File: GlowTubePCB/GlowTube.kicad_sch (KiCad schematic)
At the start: 41 parts, among them J1 Conn_01x07, P1 Solder_Pad, P2 Solder_Pad, P3 Solder_Pad, P4 Solder_Pad, P5 Solder_Pad, P6 Solder_Pad, SW1 TS-1185EC-C-D-B, SW2 TS-1185EC-C-D-B, U1 SN74LVC2T45DCUR, U2 ESP32-WROOM-32E, U3 CP2102-GMR, U4 BL1117-33CX, U5 UMH3N, U6 MSM261D4030H1CPM, U7 SS54, U8 SS54

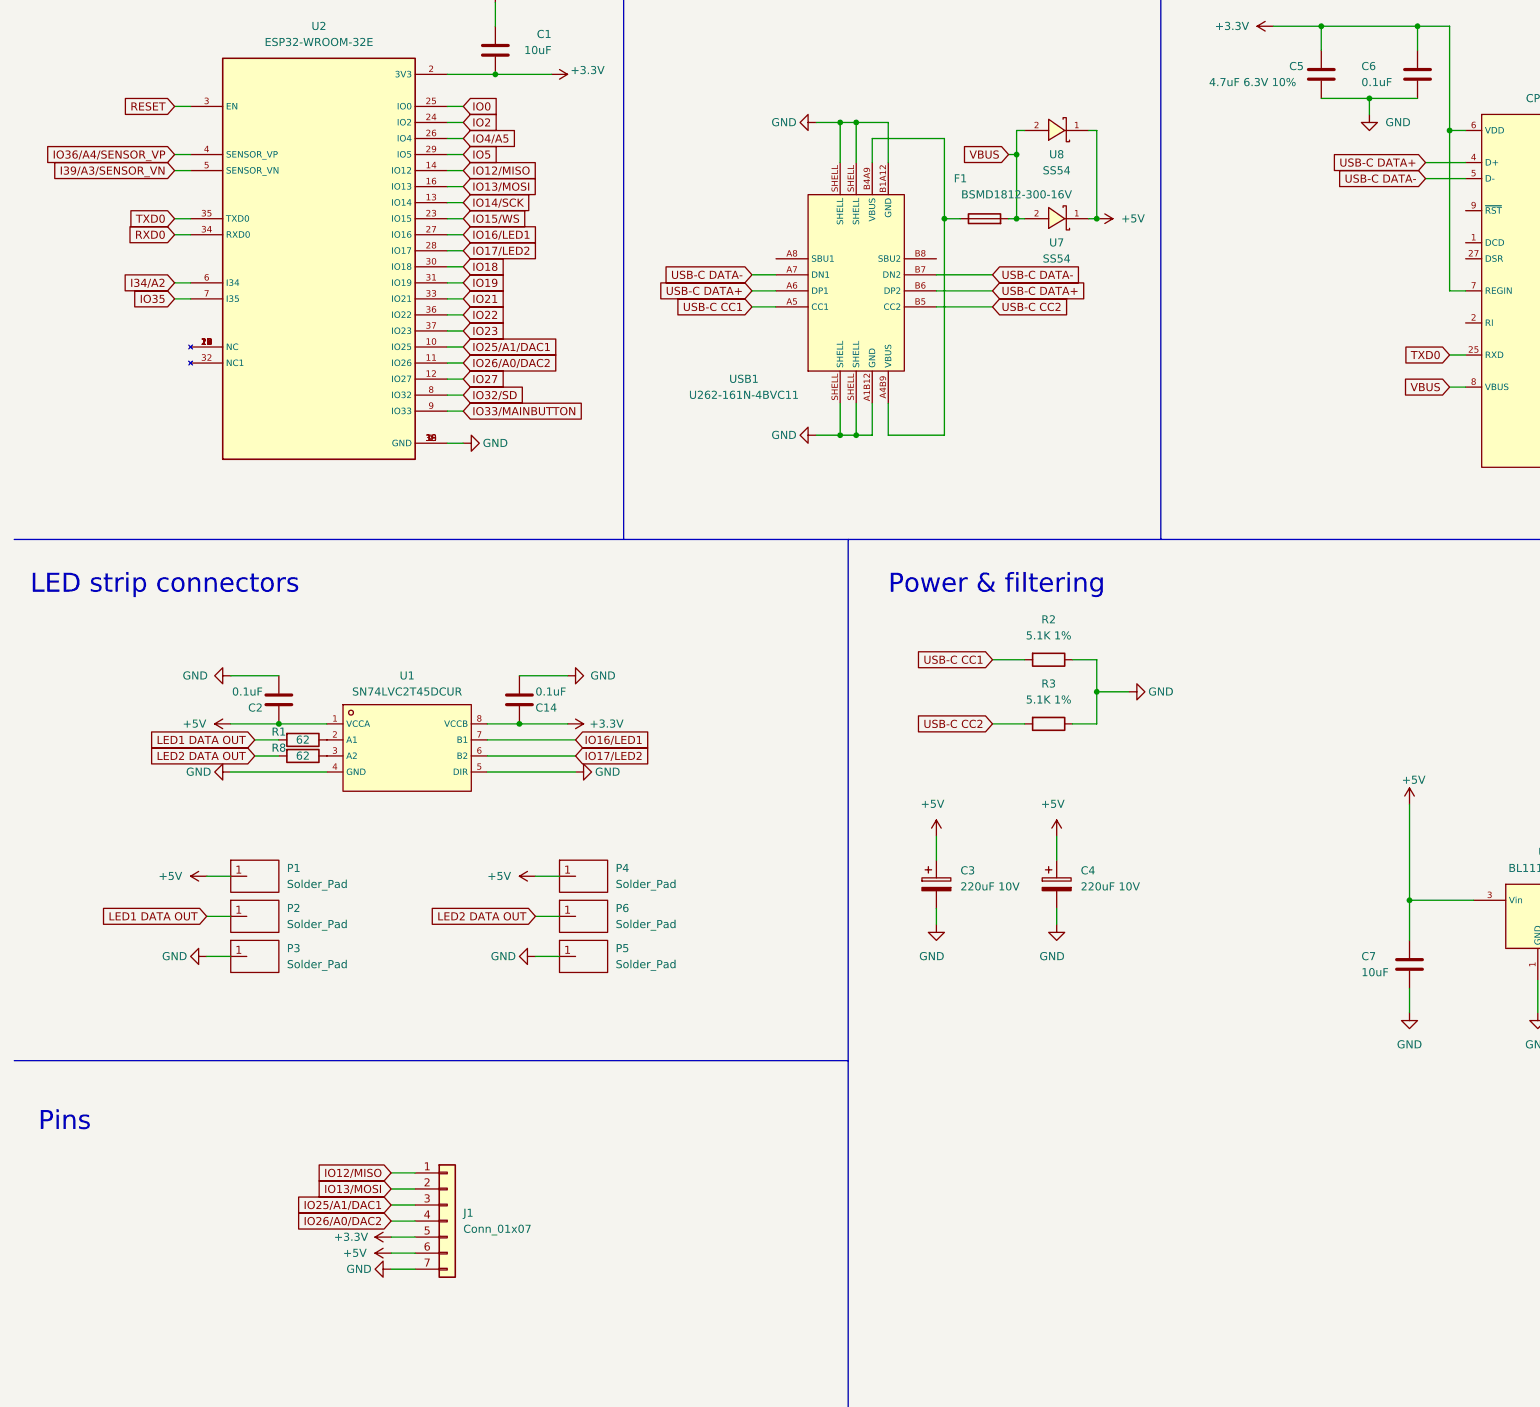
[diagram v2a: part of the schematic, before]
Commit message: added option to disconnect leds from power
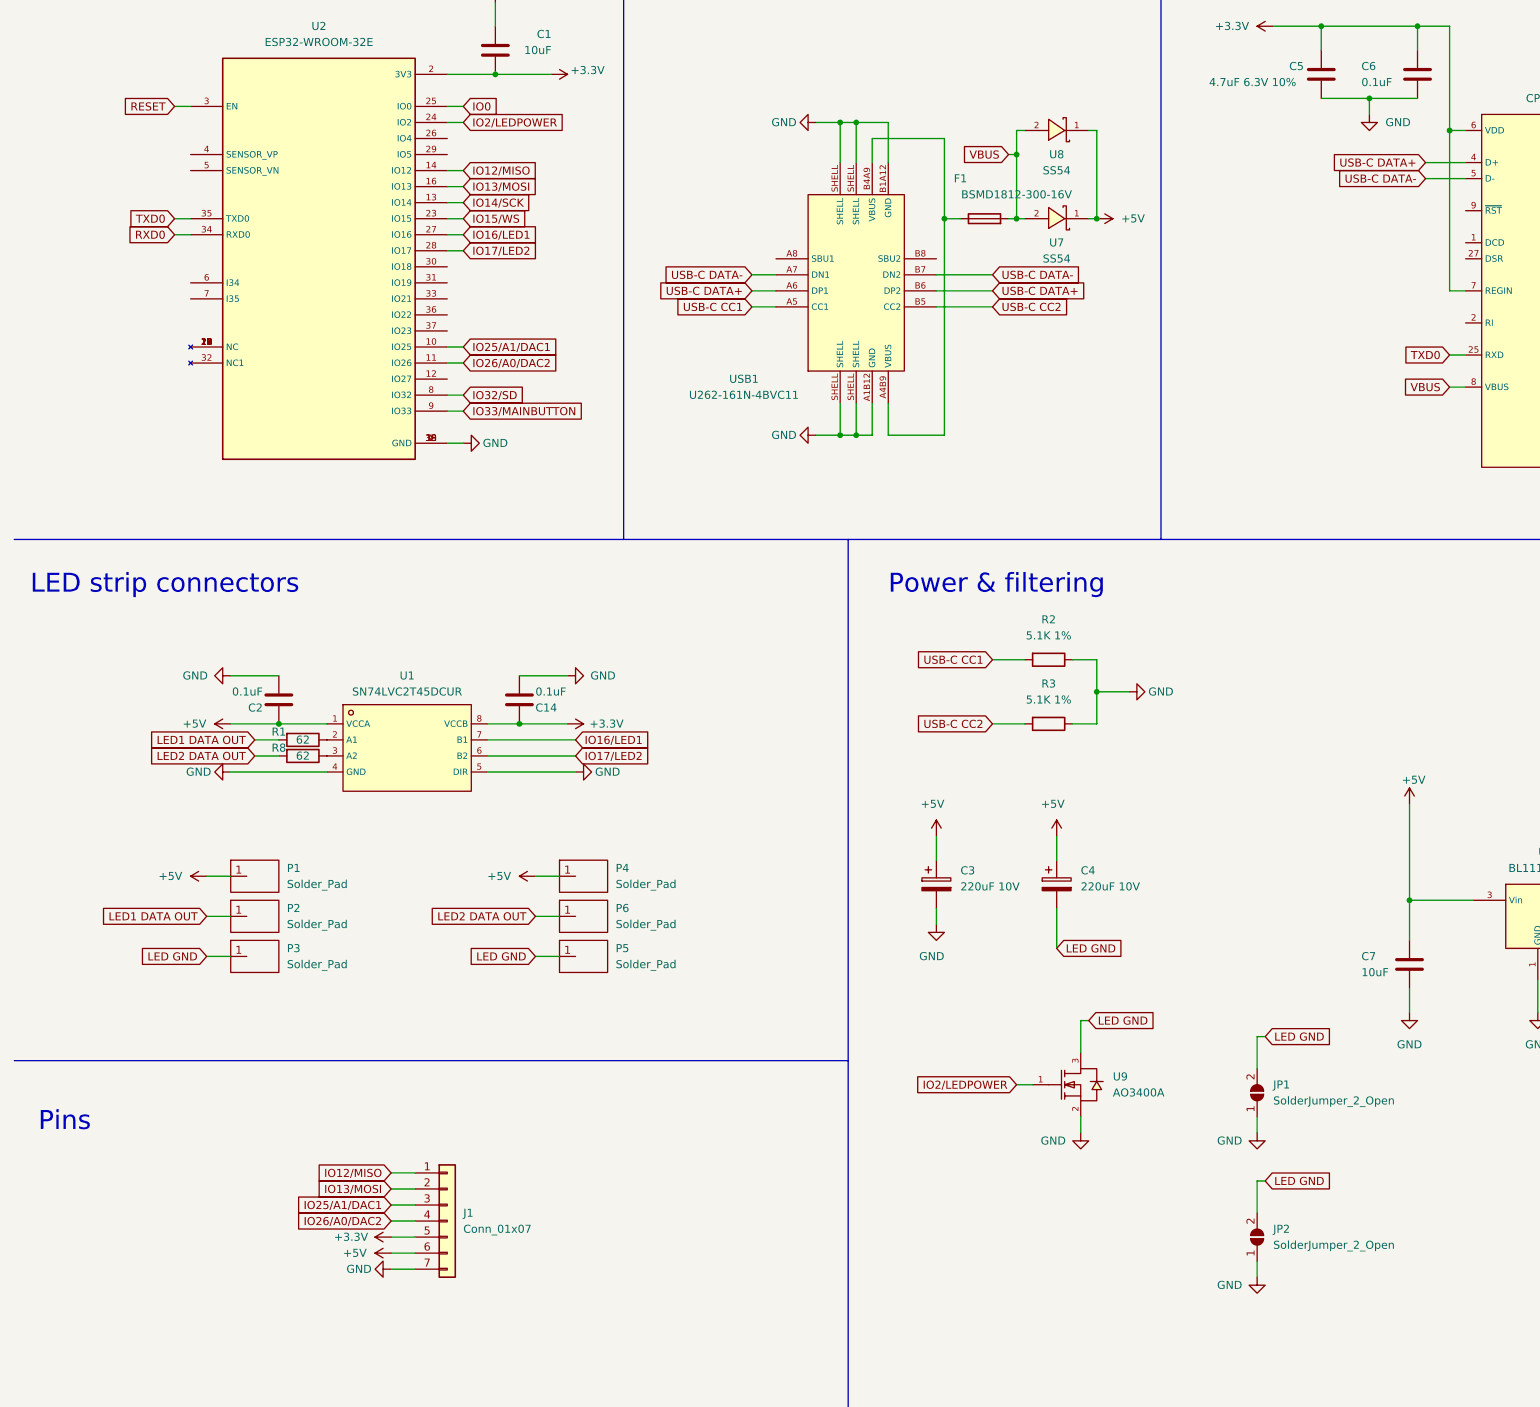
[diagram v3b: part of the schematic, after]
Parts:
- added JP1, JP2: SolderJumper_2_Open, Jumper:SolderJumper-2_P1.3mm_Open_RoundedPad1.0x1.5mm, symbol Jumper:SolderJumper_2_Open
- added U9: AO3400A, footprint:SOT-23-3_L2.9-W1.6-P1.90-LS2.8-BR, symbol MyParts:AO3400A
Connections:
- net GND: now also JP1.1 (A), JP2.1 (A), U9.2 (S); no longer C4.2, P3.1, P5.1
- net I34/A2: no longer names the net of U2.6 (I34)
- net I39/A3/SENSOR_VN: no longer names the net of U2.5 (SENSOR_VN)
- net IO18: no longer names the net of U2.30 (IO18)
- net IO19: no longer names the net of U2.31 (IO19)
- net IO2 renamed IO2/LEDPOWER
- net IO2/LEDPOWER: now also U9.1 (G)
- net IO21: no longer names the net of U2.33 (IO21)
- net IO22: no longer names the net of U2.36 (IO22)
- net IO23: no longer names the net of U2.37 (IO23)
- net IO27: no longer names the net of U2.12 (IO27)
- net IO35: no longer names the net of U2.7 (I35)
- net IO36/A4/SENSOR_VP: no longer names the net of U2.4 (SENSOR_VP)
- net IO4/A5: no longer names the net of U2.26 (IO4)
- net IO5: no longer names the net of U2.29 (IO5)
- new net LED GND: C4.2, JP1.2 (B), JP2.2 (B), P3.1, P5.1, U9.3 (D)
